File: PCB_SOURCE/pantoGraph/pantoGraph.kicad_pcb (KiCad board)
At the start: 4 copper layers, 14 x 27 mm, 33 parts, among them J101 Conn_01x01_Pin, J102 Conn_01x01_Pin, J103 Conn_01x01_Pin, J108 FFC, J201 Conn_01x03_Pin, U201 ATtiny1616-M, U301 L78L05_SOT89

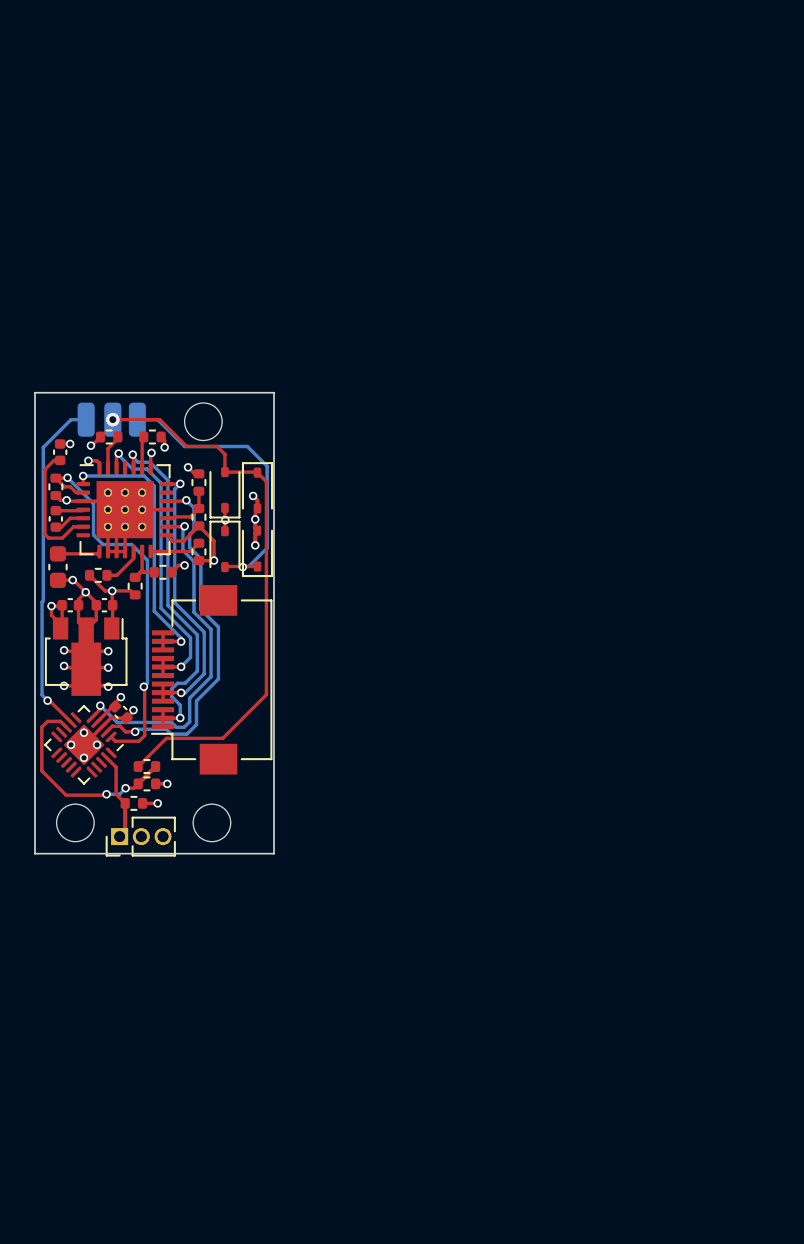
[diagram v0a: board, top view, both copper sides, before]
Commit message: upgraded servo driver code to newest standard
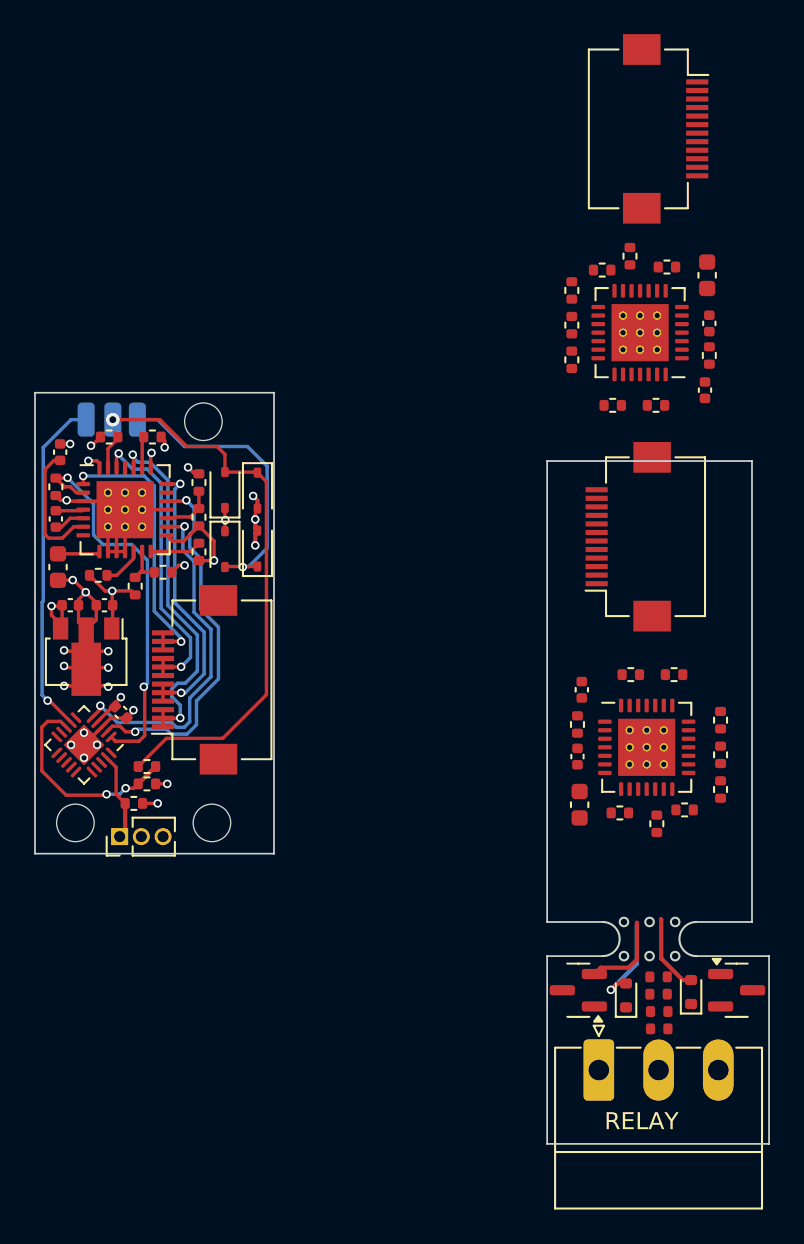
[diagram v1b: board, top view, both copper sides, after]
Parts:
- added C401: 100nF, Capacitor_SMD:C_0402_1005Metric, F.Cu at (84.3, 56.3)
- added C401: 100nF, Capacitor_SMD:C_0402_1005Metric, F.Cu at (92.0, 30.9)
- added C402: 220nF, Capacitor_SMD:C_0603_1608Metric, F.Cu at (91.9, 28.1)
- added C402: 220nF, Capacitor_SMD:C_0603_1608Metric, F.Cu at (84.4, 59.1)
- added C403: 100nF, Capacitor_SMD:C_0402_1005Metric, F.Cu at (91.7, 34.8)
- added C403: 100nF, Capacitor_SMD:C_0402_1005Metric, F.Cu at (84.5, 52.4)
- added J108: FFC, Connector_FFC-FPC:Hirose_FH12-12S-0.5SH_1x12-1MP_P0.50mm_Horizontal, F.Cu at (89.4, 19.5)
- added J108: FFC, Connector_FFC-FPC:Hirose_FH12-12S-0.5SH_1x12-1MP_P0.50mm_Horizontal, F.Cu at (87.2, 43.4)
- added R401: 100k, Resistor_SMD:R_0402_1005Metric, F.Cu at (92.0, 32.8)
- added R401: 100k, Resistor_SMD:R_0402_1005Metric, F.Cu at (84.3, 54.4)
- added R402: 100k, Resistor_SMD:R_0402_1005Metric, F.Cu at (92.7, 58.2)
- added R402: 100k, Resistor_SMD:R_0402_1005Metric, F.Cu at (83.9, 29.0)
- added R403: R_Small, Resistor_SMD:R_0402_1005Metric, F.Cu at (92.7, 56.2)
- added R403: R_Small, Resistor_SMD:R_0402_1005Metric, F.Cu at (83.9, 31.0)
- added R404: R_Small, Resistor_SMD:R_0402_1005Metric, F.Cu at (92.7, 54.2)
- added R404: R_Small, Resistor_SMD:R_0402_1005Metric, F.Cu at (83.9, 33.1)
- added R405: 100k, Resistor_SMD:R_0402_1005Metric, F.Cu at (86.8, 59.6)
- added R405: 100k, Resistor_SMD:R_0402_1005Metric, F.Cu at (89.5, 27.6)
- added R406: 1R, Resistor_SMD:R_0402_1005Metric, F.Cu at (86.3, 35.7)
- added R406: 1R, Resistor_SMD:R_0402_1005Metric, F.Cu at (89.9, 51.5)
- added R407: 1R, Resistor_SMD:R_0402_1005Metric, F.Cu at (88.9, 35.7)
- added R407: 1R, Resistor_SMD:R_0402_1005Metric, F.Cu at (87.4, 51.5)
- added R408: R_Small, Resistor_SMD:R_0402_1005Metric, F.Cu at (88.9, 60.2)
- added R408: R_Small, Resistor_SMD:R_0402_1005Metric, F.Cu at (87.4, 27.0)
- added R409: 10k, Resistor_SMD:R_0402_1005Metric, F.Cu at (85.7, 27.8)
- added R409: 10k, Resistor_SMD:R_0402_1005Metric, F.Cu at (90.6, 59.4)
- added REF**: R_0402_NO_SILK, custom_kicad_lib_sk:R_0402_NO_SILK, F.Cu at (89.0, 69.2)
- added REF**: D_SOD-523, Diode_SMD:D_SOD-523, F.Cu at (90.9, 70.1)
- added REF**: mousebite, custom_kicad_lib_sk:mousebite, F.Cu at (88.5, 67.0)
- added REF**: D_SOD-523, Diode_SMD:D_SOD-523, F.Cu at (87.1, 70.3)
- added REF**: R_0402_NO_SILK, custom_kicad_lib_sk:R_0402_NO_SILK, F.Cu at (89.1, 71.2)
- added REF**: SOT-23, Package_TO_SOT_SMD:SOT-23, F.Cu at (93.6, 70.0)
- added REF**: R_0402_NO_SILK, custom_kicad_lib_sk:R_0402_NO_SILK, F.Cu at (89.0, 70.2)
- added REF**: SOT-23, Package_TO_SOT_SMD:SOT-23, F.Cu at (84.3, 70.0)
- added REF**: R_0402_NO_SILK, custom_kicad_lib_sk:R_0402_NO_SILK, F.Cu at (89.1, 72.3)
- added RELAY: PhoenixContact_MC_1,5_3-G-3.5_1x03_P3.50mm_Horizontal, Connector_Phoenix_MC:PhoenixContact_MC_1,5_3-G-3.5_1x03_P3.50mm_Horizontal, F.Cu at (85.5, 74.7)
- added U401: ~, custom_kicad_lib_sk:a4988, F.Cu at (87.9, 31.5)
- added U401: ~, custom_kicad_lib_sk:a4988, F.Cu at (88.3, 55.8)
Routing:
- net (no net): track 0.00 -> 15.1 mm, vias 0 -> 1
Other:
- board size 14 x 27 mm -> 43 x 44 mm
